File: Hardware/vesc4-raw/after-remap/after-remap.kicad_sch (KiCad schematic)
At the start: 26 parts, among them K1 SERVO, P1 HALL/Encoder, P101 CANBUS, P3 PWR_COMM, P4 IN+, P5 IN-, P6 MOTOR1, P7 MOTOR2, P9 MOTOR3

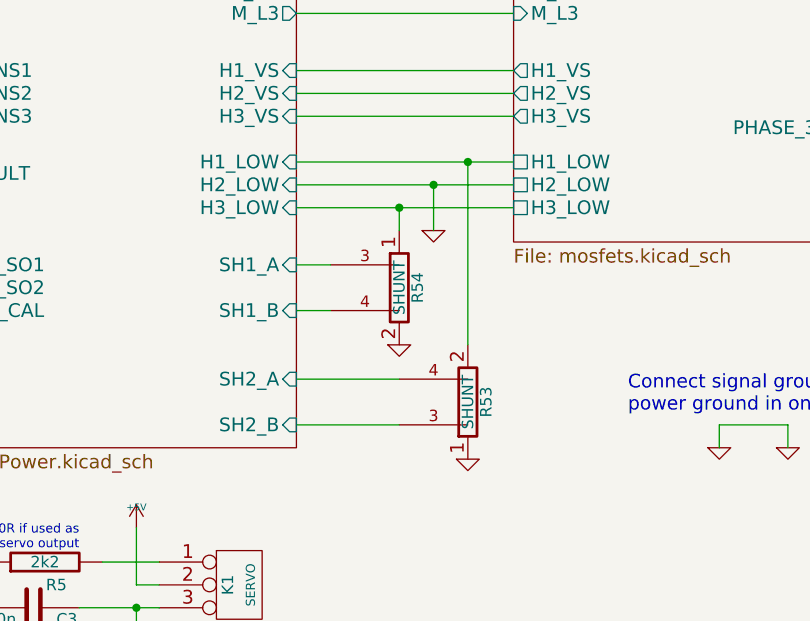
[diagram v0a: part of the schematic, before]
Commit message: checkpoint ganti shunt
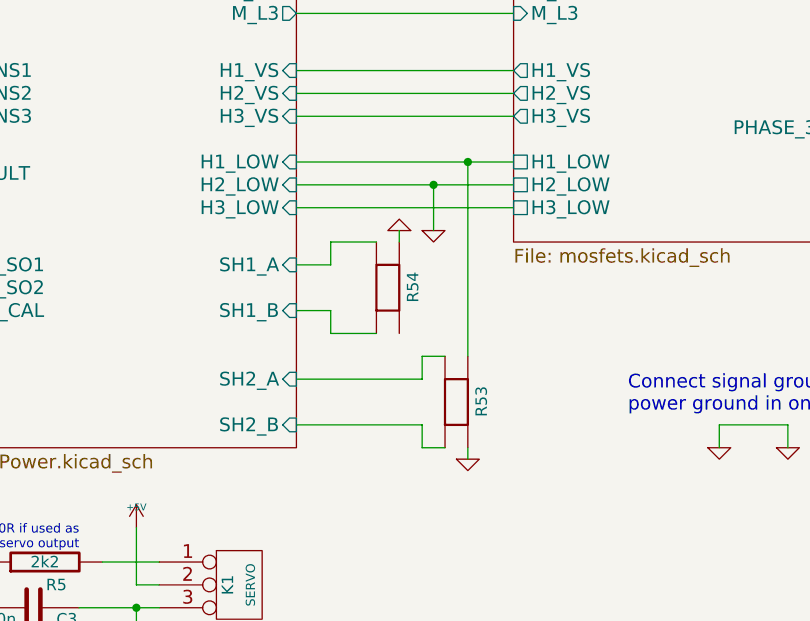
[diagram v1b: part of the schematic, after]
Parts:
- removed R53: SHUNT, CRF1:WSLP2726, symbol vesc4-legacy:SHUNT_4
- removed R54: SHUNT, CRF1:WSLP2726, symbol vesc4-legacy:SHUNT_3
- added R53, R54: WSLP27262L000FEA, Library:C2076510, symbol Library:WSLP27262L000FEA
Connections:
- net GND: now also R53.3, R54.4
- net Mosfet driver/H1_LOW: now also R53.4
- net Mosfet driver/SH1_A: now also R54.2
- net Mosfet driver/SH1_B: now also R54.1
- net Mosfet driver/SH2_A: now also R53.2
- net Mosfet driver/SH2_B: now also R53.1

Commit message: ganti shunt
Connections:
- net Mosfet driver/H3_LOW: now also R54.3
- net Mosfet driver/SH1_A: now also R54.1; no longer R54.2
- net Mosfet driver/SH1_B: now also R54.2; no longer R54.1
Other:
- moved on the sheet: R54
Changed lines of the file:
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@@
 	)
 	(junction
+		(at 207.01 101.6)
+		(diameter 0)
+		(color 0 0 0 0)
+	)
+	(junction
 		(at 16.51 82.55)
 		(diameter 0)
@@
 	(wire
 		(pts
-			(xy 199.39 113.03) (xy 195.58 113.03)
+			(xy 195.58 113.03) (xy 201.93 113.03)
 		)
 		(stroke
@@
 	(wire
 		(pts
-			(xy 207.01 104.14) (xy 207.01 105.41)
+			(xy 195.58 86.36) (xy 219.71 86.36)
 		)
 		(stroke
@@
 	(wire
 		(pts
-			(xy 195.58 86.36) (xy 219.71 86.36)
+			(xy 204.47 105.41) (xy 204.47 104.14)
 		)
 		(stroke
@@
 	(wire
 		(pts
+			(xy 199.39 104.14) (xy 203.2 104.14)
+		)
+		(stroke
+			(width 0)
+			(type default)
+		)
+	)
+	(wire
+		(pts
+			(xy 207.01 115.57) (xy 207.01 101.6)
+		)
+		(stroke
+			(width 0)
+			(type default)
+		)
+	)
+	(wire
+		(pts
 			(xy 34.29 74.93) (xy 54.61 74.93)
 		)
@@
 	(wire
 		(pts
-			(xy 199.39 105.41) (xy 204.47 105.41)
+			(xy 231.14 38.1) (xy 231.14 35.56)
 		)
 		(stroke
@@
 	(wire
 		(pts
-			(xy 231.14 38.1) (xy 231.14 35.56)
+			(xy 203.2 104.14) (xy 203.2 115.57)
 		)
 		(stroke
@@
 	(wire
 		(pts
-			(xy 147.32 140.97) (xy 160.02 140.97)
+			(xy 199.39 104.14) (xy 199.39 107.95)
 		)
 		(stroke
@@
 	(wire
 		(pts
-			(xy 147.32 97.79) (xy 157.48 97.79)
+			(xy 147.32 140.97) (xy 160.02 140.97)
 		)
 		(stroke
@@
 	(wire
 		(pts
-			(xy 209.55 118.11) (xy 212.09 118.11)
+			(xy 147.32 97.79) (xy 157.48 97.79)
 		)
 		(stroke
@@
 	(wire
 		(pts
-			(xy 199.39 107.95) (xy 199.39 105.41)
-		)
-		(stroke
-			(width 0)
-			(type default)
-		)
-	)
-	(wire
-		(pts
 			(xy 199.39 107.95) (xy 195.58 107.95)
 		)
@@
 	(wire
 		(pts
-			(xy 195.58 120.65) (xy 209.55 120.65)
-		)
-		(stroke
-			(width 0)
-			(type default)
-		)
-	)
-	(wire
-		(pts
-			(xy 209.55 128.27) (xy 212.09 128.27)
-		)
-		(stroke
-			(width 0)
-			(type default)
-		)
-	)
-	(wire
-		(pts
-			(xy 199.39 115.57) (xy 204.47 115.57)
+			(xy 195.58 120.65) (xy 212.09 120.65)
 		)
 		(stroke
@@
 	(wire
 		(pts
+			(xy 212.09 120.65) (xy 212.09 118.11)
+		)
+		(stroke
+			(width 0)
+			(type default)
+		)
+	)
+	(wire
+		(pts
 			(xy 16.51 85.09) (xy 16.51 82.55)
 		)
@@
 	(wire
 		(pts
-			(xy 195.58 125.73) (xy 209.55 125.73)
+			(xy 195.58 125.73) (xy 212.09 125.73)
 		)
 		(stroke
@@
 	(wire
 		(pts
+			(xy 201.93 113.03) (xy 201.93 105.41)
+		)
+		(stroke
+			(width 0)
+			(type default)
+		)
+	)
+	(wire
+		(pts
 			(xy 35.56 85.09) (xy 40.64 85.09)
 		)
@@
 	(wire
 		(pts
-			(xy 209.55 120.65) (xy 209.55 118.11)
+			(xy 160.02 146.05) (xy 161.29 146.05)
 		)
 		(stroke
@@
 	(wire
 		(pts
-			(xy 160.02 146.05) (xy 161.29 146.05)
+			(xy 36.83 140.97) (xy 82.55 140.97)
 		)
 		(stroke
@@
 	(wire
 		(pts
-			(xy 36.83 140.97) (xy 82.55 140.97)
+			(xy 43.18 57.15) (xy 43.18 60.96)
 		)
 		(stroke
@@
 	(wire
 		(pts
-			(xy 43.18 57.15) (xy 43.18 60.96)
+			(xy 72.39 119.38) (xy 82.55 119.38)
 		)
 		(stroke
@@
 	(wire
 		(pts
-			(xy 72.39 119.38) (xy 82.55 119.38)
+			(xy 177.8 146.05) (xy 177.8 148.59)
 		)
 		(stroke
@@
 	(wire
 		(pts
-			(xy 177.8 146.05) (xy 177.8 148.59)
+			(xy 147.32 63.5) (xy 157.48 63.5)
 		)
 		(stroke
@@
 	(wire
 		(pts
-			(xy 147.32 63.5) (xy 157.48 63.5)
+			(xy 35.56 90.17) (xy 35.56 85.09)
 		)
 		(stroke
@@
 	(wire
 		(pts
-			(xy 35.56 90.17) (xy 35.56 85.09)
+			(xy 207.01 101.6) (xy 219.71 101.6)
 		)
 		(stroke
@@
 	(wire
 		(pts
-			(xy 177.8 146.05) (xy 180.34 146.05)
+			(xy 212.09 125.73) (xy 212.09 128.27)
 		)
 		(stroke
@@
 	(wire
 		(pts
-			(xy 209.55 125.73) (xy 209.55 128.27)
+			(xy 177.8 146.05) (xy 180.34 146.05)
 		)
 		(stroke
@@
 	(wire
 		(pts
-			(xy 199.39 113.03) (xy 199.39 115.57)
+			(xy 250.19 125.73) (xy 250.19 128.27)
 		)
 		(stroke
@@
 	(wire
 		(pts
-			(xy 250.19 125.73) (xy 250.19 128.27)
+			(xy 203.2 115.57) (xy 201.93 115.57)
 		)
 		(stroke
@@
 	(wire
 		(pts
-			(xy 58.42 54.61) (xy 59.69 54.61)
+			(xy 195.58 101.6) (xy 207.01 101.6)
 		)
 		(stroke
@@
 	(wire
 		(pts
-			(xy 214.63 96.52) (xy 219.71 96.52)
+			(xy 58.42 54.61) (xy 59.69 54.61)
 		)
 		(stroke
@@
 	(wire
 		(pts
-			(xy 171.45 146.05) (xy 177.8 146.05)
+			(xy 214.63 96.52) (xy 219.71 96.52)
 		)
 		(stroke
@@
 	(wire
 		(pts
-			(xy 195.58 101.6) (xy 219.71 101.6)
+			(xy 171.45 146.05) (xy 177.8 146.05)
 		)
 		(stroke
@@
 	(wire
 		(pts
+			(xy 204.47 115.57) (xy 207.01 115.57)
+		)
+		(stroke
+			(width 0)
+			(type default)
+		)
+	)
+	(wire
+		(pts
 			(xy 149.86 149.86) (xy 149.86 156.21)
 		)
@@
 		)
 	)
+	(hierarchical_label "Q7_S"
+		(shape input)
+		(at 220.98 172.72 0)
+		(effects
+			(font
+				(size 1.27 1.27)
+			)
+			(justify left)
+		)
+	)
 	(symbol
 		(lib_name "CONN_6_2")
@@
 		(lib_name "GND-RESCUE-BLDC_4_17")
 		(lib_id "vesc4-legacy:GND-RESCUE-BLDC_4_17")
-		(at 207.01 104.14 180)
+		(at 204.47 104.14 180)
 		(unit 1)
 		(exclude_from_sim no)
@@
 		(dnp no)
 		(property "Reference" "#PWR020"
-			(at 207.01 104.14 0)
+			(at 204.47 104.14 0)
 			(effects
 				(font
@@
 		)
 		(property "Value" "GND"
-			(at 207.01 102.362 0)
+			(at 204.47 102.362 0)
 			(effects
 				(font
@@
 		)
 		(property "Footprint" ""
-			(at 207.01 104.14 0)
+			(at 204.47 104.14 0)
 			(effects
 				(font
@@
 		)
 		(property "Datasheet" ""
-			(at 207.01 104.14 0)
+			(at 204.47 104.14 0)
 			(effects
 				(font
@@
 		)
 		(property "Description" ""
-			(at 207.01 104.14 0)
+			(at 204.47 104.14 0)
 			(effects
 				(font
@@
 	(symbol
 		(lib_id "Library:WSLP27262L000FEA")
-		(at 205.74 110.49 90)
+		(at 203.2 110.49 90)
 		(unit 1)
 		(exclude_from_sim no)
@@
 		(dnp no)
 		(property "Reference" "R54"
-			(at 208.534 108.712 0)
+			(at 205.994 108.712 0)
 			(effects
 				(font
@@
 		)
 		(property "Value" "WSLP27262L000FEA"
-			(at 208.28 111.7599 90)
+			(at 205.74 111.7599 90)
 			(effects
 				(font
@@
 		)
 		(property "Footprint" "Library:C2076510"
-			(at 205.74 110.49 0)
+			(at 203.2 110.49 0)
 			(effects
 				(font
@@
 		)
 		(property "Datasheet" ""
-			(at 205.74 110.49 0)
+			(at 203.2 110.49 0)
 			(effects
 				(font
@@
 		)
 		(property "Description" ""
-			(at 205.74 110.49 0)
+			(at 203.2 110.49 0)
 			(effects
 				(font
@@
 		)
 		(property "Manufacturer Part" "WSLP27262L000FEA"
-			(at 205.74 110.49 0)
+			(at 203.2 110.49 0)
 			(effects
 				(font
@@
 		)
 		(property "Manufacturer" "VISHAY(威世)"
-			(at 205.74 110.49 0)
+			(at 203.2 110.49 0)
 			(effects
 				(font
@@
 		)
 		(property "Supplier Part" "C2076510"
-			(at 205.74 110.49 0)
+			(at 203.2 110.49 0)
 			(effects
 				(font
@@
 		)
 		(property "Supplier" "LCSC"
-			(at 205.74 110.49 0)
+			(at 203.2 110.49 0)
 			(effects
 				(font

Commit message: changed USB
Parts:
- removed U4: ~, EasyEDA_Lib:MICRO-USB-SMD_MICROUSB-5P-M, symbol EasyEDA_Lib:MICRO USB 5P贴板公头四脚贴带卡勾
- added U4: MICROQTJ, symbol Library:MICROQTJ
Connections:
- net D+: now also U4.3 (D+)
- net D-: now also U4.2 (D-)
- net GND: now also U4.5 (GND), U4.6 (SH1), U4.7 (SH2), U4.8 (SH3), U4.9 (SH4)
- net at D6.2 (A): now also U4.1 (VBUS)

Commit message: sebelum ganti kapasitor 1206
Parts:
- U4: footprint (none) -> Library:MICRO-USB-SMD_MICROQTJ-5P
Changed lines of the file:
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@@
 			)
 		)
-		(property "Footprint" ""
+		(property "Footprint" "Library:MICRO-USB-SMD_MICROQTJ-5P"
 			(at 24.13 80.01 0)
 			(effects
